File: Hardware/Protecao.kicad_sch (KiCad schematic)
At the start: 7 parts, among them U9 Opamp_Quad

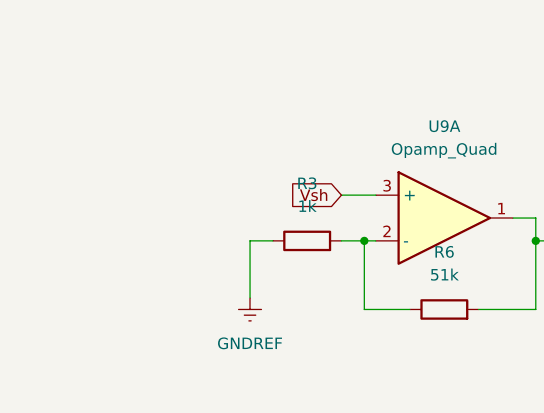
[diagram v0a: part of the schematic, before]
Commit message: 2026_07_09
Feitas simulações da corrente do gate e escolha de um novo gate driver
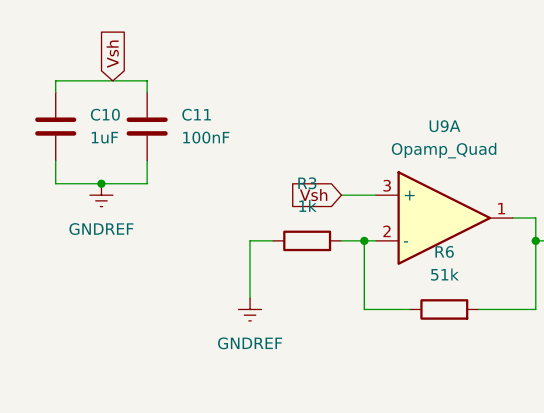
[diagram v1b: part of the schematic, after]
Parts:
- added C10: 1uF, symbol Device:C
- added C11: 100nF, symbol Device:C
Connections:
- net GNDREF: now also C10.2, C11.2
- net Vsh: now also C10.1, C11.1

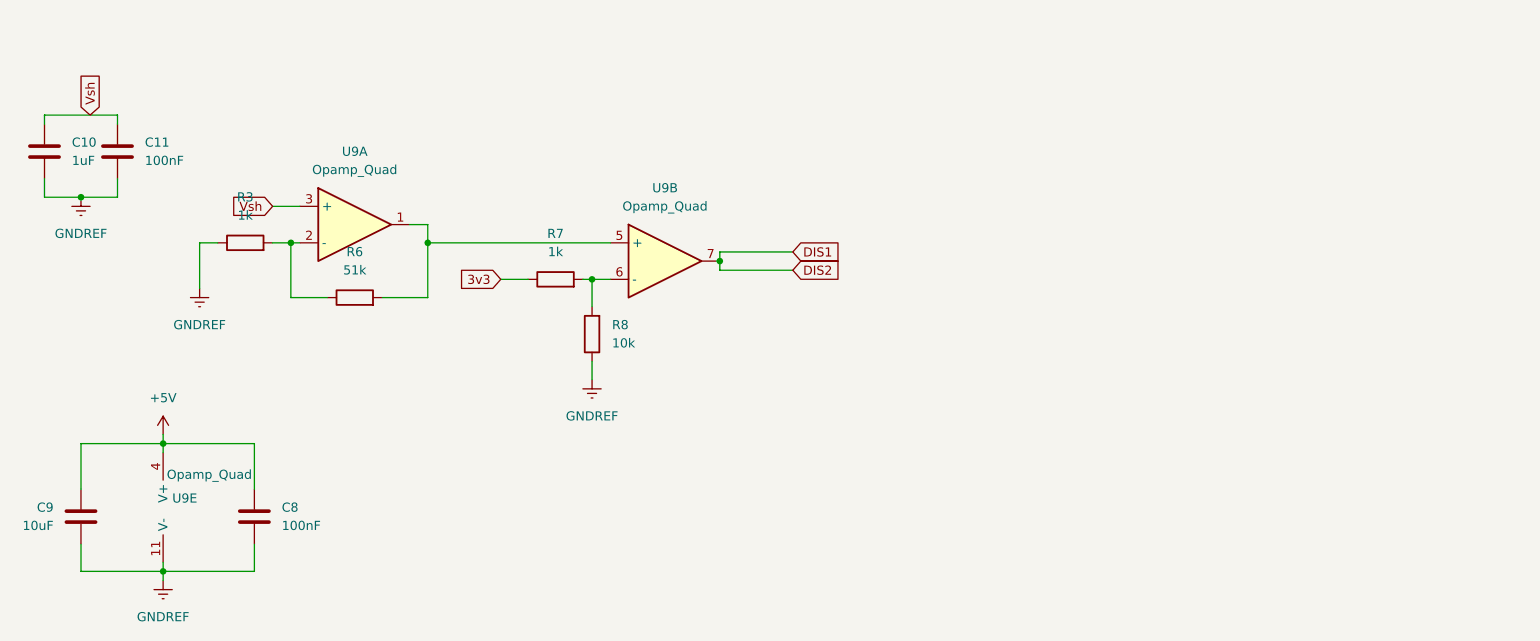
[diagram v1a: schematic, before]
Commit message: 2026_07_22
Finalizada a PCB para fazer na fresa do IFSC
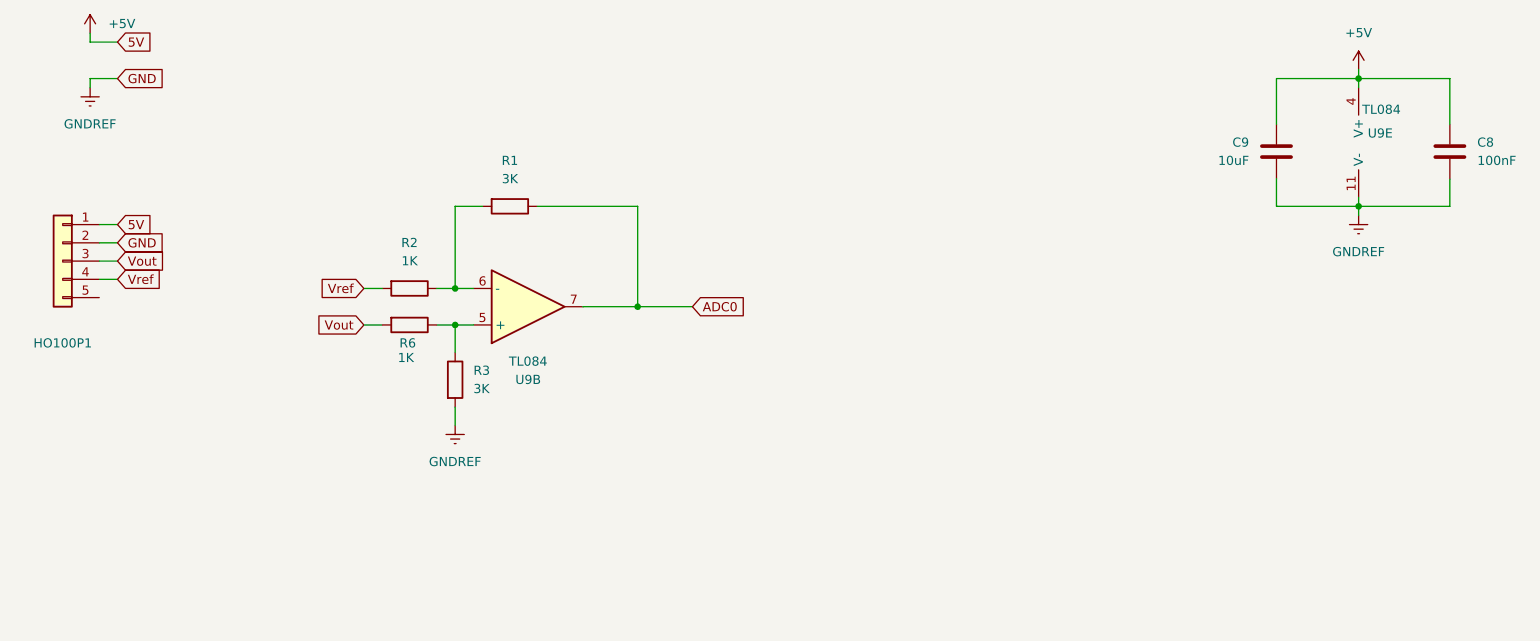
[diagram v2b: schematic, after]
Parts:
- removed C10: 1uF, symbol Device:C
- removed C11: 100nF, symbol Device:C
- removed R7: 1k, Resistor_SMD:R_0805_2012Metric_Pad1.20x1.40mm_HandSolder, symbol Device:R
- removed R8: 10k, Resistor_SMD:R_0805_2012Metric_Pad1.20x1.40mm_HandSolder, symbol Device:R
- removed unit 1 of U9
- added HO100P1: Conn_01x05, Connector_Molex:Molex_KK-254_AE-6410-05A_1x05_P2.54mm_Vertical, symbol Connector_Generic:Conn_01x05
- added R1: 3K, Resistor_SMD:R_0805_2012Metric_Pad1.20x1.40mm_HandSolder, symbol Device:R
- added R2: 1K, Resistor_SMD:R_0805_2012Metric_Pad1.20x1.40mm_HandSolder, symbol Device:R
- R3: value 1k -> 3K
- R6: value 51k -> 1K
- U9: value Opamp_Quad -> TL084
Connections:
- net +5V: now also HO100P1.1 (Pin_1)
- net GNDREF: now also R3.2, HO100P1.2 (Pin_2); no longer R3.1
- net at U9.6 (-): now also R1.2, R2.1
- net at U9.5 (+): now also R3.1, R6.1; no longer R6.2
- net DIS1 renamed ADC0
- net ADC0: now also R1.1
- new net Vout: HO100P1.3 (Pin_3), R6.2
- new net Vref: HO100P1.4 (Pin_4), R2.2
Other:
- moved on the sheet: C8, C9, U9B, U9E
